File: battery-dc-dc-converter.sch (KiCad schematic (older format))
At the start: 26 parts, among them J1 Conn_01x02, J2 Conn_01x02, U1 LMR16030

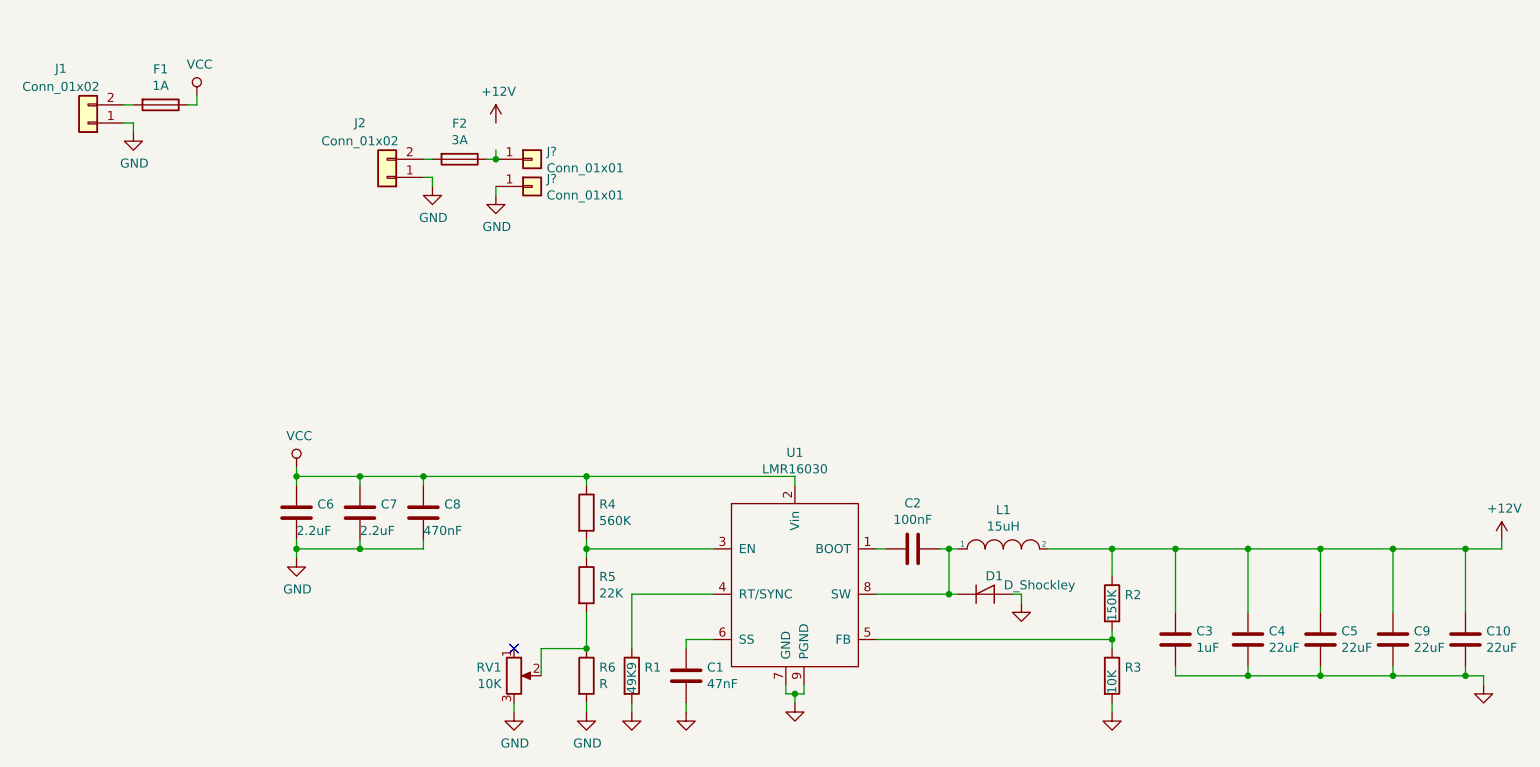
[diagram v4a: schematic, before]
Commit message: Panalized PCBs
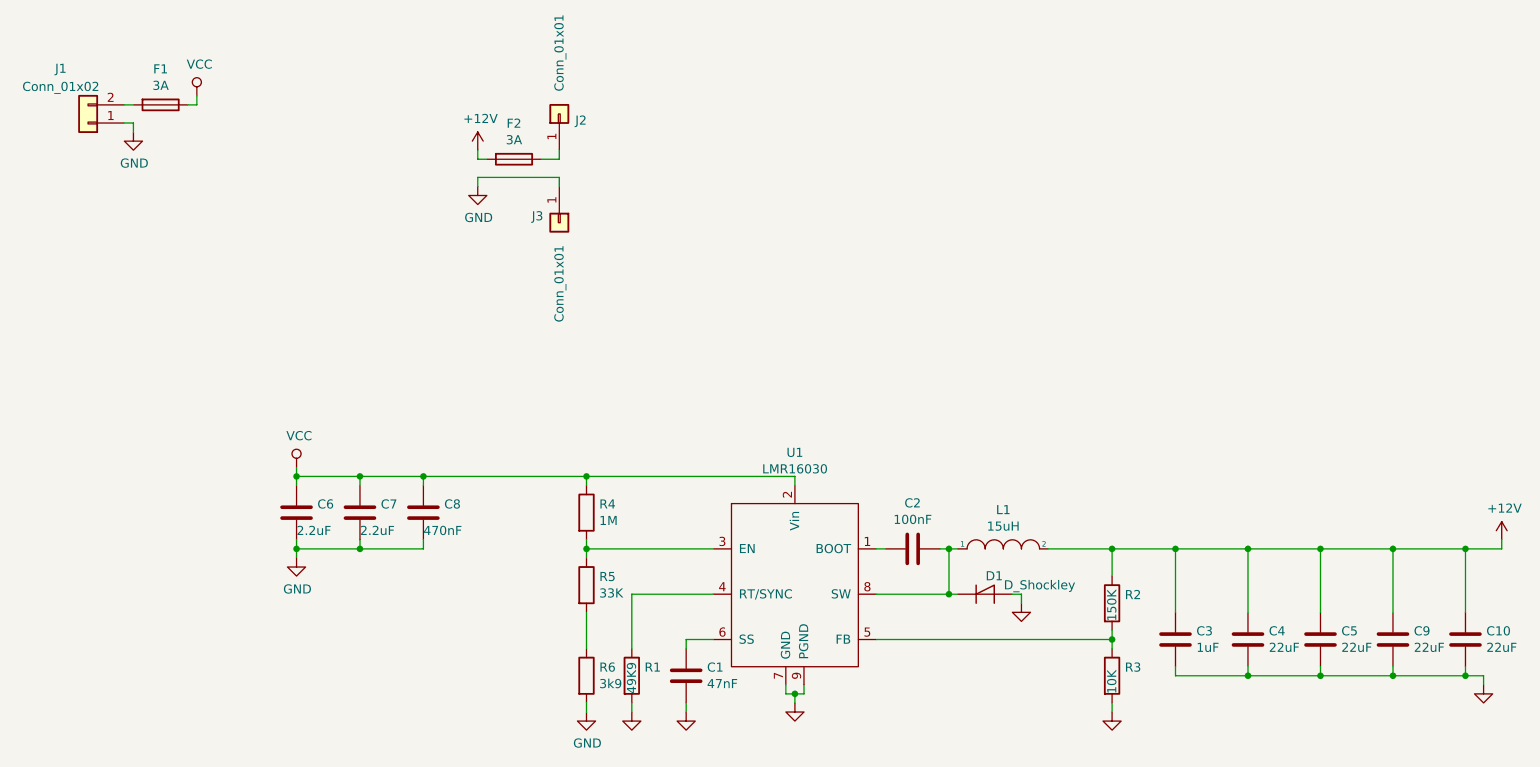
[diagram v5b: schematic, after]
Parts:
- removed J2: Conn_01x02, Connector_JST:JST_XH_B2B-XH-A_1x02_P2.50mm_Vertical, symbol Connector_Generic:Conn_01x02
- removed J? (x2): Conn_01x01, Connector_Wire:SolderWirePad_1x01_SMD_5x10mm, symbol Connector_Generic:Conn_01x01
- removed RV1: 10K, Potentiometer_THT:Potentiometer_Vishay_T73XX_Horizontal, symbol Device:R_POT
- added J2, J3: Conn_01x01, battery-dc-dc-converter:hole-pad, symbol Connector_Generic:Conn_01x01
- F1: value 1A -> 3A; LCSC C182305 -> C182441
- R4: value 560K -> 1M; LCSC C15785 -> C17514
- R5: value 22K -> 33K; LCSC C17560 -> C17633
- R6: value R -> 3k9; LCSC C17477 -> C17614
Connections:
- net +12V: now also F2.2
- net GND: now also J3.1 (Pin_1)
- net at F2.1: now also J2.1 (Pin_1)
- no-connect marks 1 -> 0
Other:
- moved on the sheet: F2
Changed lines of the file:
@@
 	1200 1000 1250 1000
-$Comp
-L Connector_Generic:Conn_01x02 J2
-U 1 1 5F4E1407
-P 2650 1400
-F 0 "J2" H 2800 1100 50  0000 C CNN
-F 1 "Conn_01x02" H 2800 1200 50  0000 C CNN
-F 2 "Connector_JST:JST_XH_B2B-XH-A_1x02_P2.50mm_Vertical" H 2650 1400 50  0001 C CNN
-F 3 "~" H 2650 1400 50  0001 C CNN
-F 4 "C8465" H 2650 1400 50  0001 C CNN "LCSC"
-	1    2650 1400
-	-1   0    0    1
-$EndComp
 $Comp
 L power:GND #PWR0111
 U 1 1 5F4E19F6
-P 2900 1450
-F 0 "#PWR0111" H 2900 1200 50  0001 C CNN
-F 1 "GND" H 2905 1277 50  0000 C CNN
-F 2 "" H 2900 1450 50  0001 C CNN
-F 3 "" H 2900 1450 50  0001 C CNN
-	1    2900 1450
+P 3150 1450
+F 0 "#PWR0111" H 3150 1200 50  0001 C CNN
+F 1 "GND" H 3155 1277 50  0000 C CNN
+F 2 "" H 3150 1450 50  0001 C CNN
+F 3 "" H 3150 1450 50  0001 C CNN
+	1    3150 1450
 	1    0    0    -1
 $EndComp
@@
 L power:+12V #PWR0112
 U 1 1 5F4E22CD
-P 3250 1100
-F 0 "#PWR0112" H 3250 950 50  0001 C CNN
-F 1 "+12V" H 3265 1273 50  0000 C CNN
-F 2 "" H 3250 1100 50  0001 C CNN
-F 3 "" H 3250 1100 50  0001 C CNN
-	1    3250 1100
-	1    0    0    -1
-$EndComp
-Wire Wire Line
-	2850 1300 2900 1300
-Wire Wire Line
-	2850 1400 2900 1400
-Wire Wire Line
-	2900 1400 2900 1450
+P 3150 1250
+F 0 "#PWR0112" H 3150 1100 50  0001 C CNN
+F 1 "+12V" H 3165 1423 50  0000 C CNN
+F 2 "" H 3150 1250 50  0001 C CNN
+F 3 "" H 3150 1250 50  0001 C CNN
+	1    3150 1250
+	1    0    0    -1
+$EndComp
 Wire Wire Line
 	1250 1100 1250 1150
@@
 P 1400 1000
 F 0 "F1" V 1203 1000 50  0000 C CNN
-F 1 "1A" V 1294 1000 50  0000 C CNN
+F 1 "3A" V 1294 1000 50  0000 C CNN
 F 2 "Fuse:Fuse_1206_3216Metric_Pad1.42x1.75mm_HandSolder" V 1330 1000 50  0001 C CNN
 F 3 "~" H 1400 1000 50  0001 C CNN
-F 4 "C182305" H 1400 1000 50  0001 C CNN "LCSC"
+F 4 "C182441" H 1400 1000 50  0001 C CNN "LCSC"
 	1    1400 1000
 	0    1    1    0
@@
 L Device:Fuse F2
 U 1 1 5FB27E6C
-P 3050 1300
-F 0 "F2" V 2853 1300 50  0000 C CNN
-F 1 "3A" V 2944 1300 50  0000 C CNN
-F 2 "Fuse:Fuse_1206_3216Metric_Pad1.42x1.75mm_HandSolder" V 2980 1300 50  0001 C CNN
-F 3 "~" H 3050 1300 50  0001 C CNN
-F 4 "C182441" H 3050 1300 50  0001 C CNN "LCSC"
-	1    3050 1300
+P 3350 1300
+F 0 "F2" V 3153 1300 50  0000 C CNN
+F 1 "3A" V 3244 1300 50  0000 C CNN
+F 2 "Fuse:Fuse_1206_3216Metric_Pad1.42x1.75mm_HandSolder" V 3280 1300 50  0001 C CNN
+F 3 "~" H 3350 1300 50  0001 C CNN
+F 4 "C182441" H 3350 1300 50  0001 C CNN "LCSC"
+	1    3350 1300
 	0    1    1    0
 $EndComp
-Wire Wire Line
-	3200 1300 3250 1300
-Wire Wire Line
-	3250 1300 3250 1250
 $Comp
 L Device:R R4
@@
 P 3750 3250
 F 0 "R4" H 3820 3296 50  0000 L CNN
-F 1 "560K" H 3820 3205 50  0000 L CNN
+F 1 "1M" H 3820 3205 50  0000 L CNN
 F 2 "Resistor_SMD:R_0805_2012Metric_Pad1.20x1.40mm_HandSolder" V 3680 3250 50  0001 C CNN
 F 3 "~" H 3750 3250 50  0001 C CNN
-F 4 "C15785" H 3750 3250 50  0001 C CNN "LCSC"
+F 4 "C17514" H 3750 3250 50  0001 C CNN "LCSC"
 	1    3750 3250
 	1    0    0    -1
@@
 P 3750 3650
 F 0 "R5" H 3820 3696 50  0000 L CNN
-F 1 "22K" H 3820 3605 50  0000 L CNN
+F 1 "33K" H 3820 3605 50  0000 L CNN
 F 2 "Resistor_SMD:R_0805_2012Metric_Pad1.20x1.40mm_HandSolder" V 3680 3650 50  0001 C CNN
 F 3 "~" H 3750 3650 50  0001 C CNN
-F 4 "C17560" H 3750 3650 50  0001 C CNN "LCSC"
+F 4 "C17633" H 3750 3650 50  0001 C CNN "LCSC"
 	1    3750 3650
 	1    0    0    -1
@@
 Wire Wire Line
 	4900 3050 4900 3100
-$Comp
-L Device:R_POT RV1
-U 1 1 5FB5C125
-P 3350 4150
-F 0 "RV1" H 3281 4196 50  0000 R CNN
-F 1 "10K" H 3281 4105 50  0000 R CNN
-F 2 "Potentiometer_THT:Potentiometer_Vishay_T73XX_Horizontal" H 3350 4150 50  0001 C CNN
-F 3 "~" H 3350 4150 50  0001 C CNN
-F 4 "C118898" H 3350 4150 50  0001 C CNN "LCSC"
-	1    3350 4150
-	1    0    0    -1
-$EndComp
-NoConn ~ 3350 4000
 Wire Wire Line
 	3750 4000 3750 3800
@@
 P 3750 4150
 F 0 "R6" H 3820 4196 50  0000 L CNN
-F 1 "R" H 3820 4105 50  0000 L CNN
+F 1 "3k9" H 3820 4105 50  0000 L CNN
 F 2 "Resistor_SMD:R_0805_2012Metric_Pad1.20x1.40mm_HandSolder" V 3680 4150 50  0001 C CNN
 F 3 "~" H 3750 4150 50  0001 C CNN
-F 4 "C17477" H 3750 4150 50  0001 C CNN "LCSC"
+F 4 "C17614" H 3750 4150 50  0001 C CNN "LCSC"
 	1    3750 4150
 	1    0    0    -1
 $EndComp
-Connection ~ 3750 4000
-Wire Wire Line
-	3500 4000 3500 4150
-Wire Wire Line
-	3500 4000 3750 4000
-$Comp
-L power:GND #PWR0115
-U 1 1 5FB7F217
-P 3350 4350
-F 0 "#PWR0115" H 3350 4100 50  0001 C CNN
-F 1 "GND" H 3355 4177 50  0000 C CNN
-F 2 "" H 3350 4350 50  0001 C CNN
-F 3 "" H 3350 4350 50  0001 C CNN
-	1    3350 4350
-	1    0    0    -1
-$EndComp
 Wire Wire Line
 	3750 4300 3750 4350
-Wire Wire Line
-	3350 4350 3350 4300
-$Comp
-L Connector_Generic:Conn_01x01 J?
-U 1 1 60369738
-P 3450 1300
-F 0 "J?" H 3530 1342 50  0000 L CNN
-F 1 "Conn_01x01" H 3530 1251 50  0000 L CNN
-F 2 "Connector_Wire:SolderWirePad_1x01_SMD_5x10mm" H 3450 1300 50  0001 C CNN
-F 3 "~" H 3450 1300 50  0001 C CNN
-	1    3450 1300
-	1    0    0    -1
-$EndComp
-Connection ~ 3250 1300
-$Comp
-L Connector_Generic:Conn_01x01 J?
-U 1 1 60369BF3
-P 3450 1450
-F 0 "J?" H 3530 1492 50  0000 L CNN
-F 1 "Conn_01x01" H 3530 1401 50  0000 L CNN
-F 2 "Connector_Wire:SolderWirePad_1x01_SMD_5x10mm" H 3450 1450 50  0001 C CNN
-F 3 "~" H 3450 1450 50  0001 C CNN
-	1    3450 1450
-	1    0    0    -1
-$EndComp
-$Comp
-L power:GND #PWR?
-U 1 1 6036A147
-P 3250 1500
-F 0 "#PWR?" H 3250 1250 50  0001 C CNN
-F 1 "GND" H 3255 1327 50  0000 C CNN
-F 2 "" H 3250 1500 50  0001 C CNN
-F 3 "" H 3250 1500 50  0001 C CNN
-	1    3250 1500
-	1    0    0    -1
-$EndComp
-Wire Wire Line
-	3250 1500 3250 1450
+$Comp
+L Connector_Generic:Conn_01x01 J2
+U 1 1 603798F3
+P 3600 1050
+F 0 "J2" V 3564 962 50  0000 R CNN
+F 1 "Conn_01x01" H 4150 1050 50  0000 R CNN
+F 2 "battery-dc-dc-converter:hole-pad" H 3600 1050 50  0001 C CNN
+F 3 "~" H 3600 1050 50  0001 C CNN
+	1    3600 1050
+	0    -1   -1   0
+$EndComp
+$Comp
+L Connector_Generic:Conn_01x01 J3
+U 1 1 6037DD21
+P 3600 1650
+F 0 "J3" V 3564 1562 50  0000 R CNN
+F 1 "Conn_01x01" H 4150 1650 50  0000 R CNN
+F 2 "battery-dc-dc-converter:hole-pad" H 3600 1650 50  0001 C CNN
+F 3 "~" H 3600 1650 50  0001 C CNN
+	1    3600 1650
+	0    1    1    0
+$EndComp
+Wire Wire Line
+	3150 1450 3150 1400
+Wire Wire Line
+	3150 1400 3600 1400
+Wire Wire Line
+	3600 1400 3600 1450
+Wire Wire Line
+	3150 1250 3150 1300
+Wire Wire Line
+	3150 1300 3200 1300
+Wire Wire Line
+	3500 1300 3600 1300
+Wire Wire Line
+	3600 1300 3600 1250
 $EndSCHEMATC

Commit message: Improved EMI
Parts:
- removed C10, C9: 22uF, Capacitor_SMD:C_0805_2012Metric, symbol Device:C
- added R7: 3R3, Resistor_SMD:R_0805_2012Metric, symbol Device:R
- C10: renamed from C6; footprint Capacitor_SMD:C_1206_3216Metric -> Capacitor_SMD:C_1210_3225Metric; LCSC C50254 -> C106115
- C11: renamed from C7; footprint Capacitor_SMD:C_1206_3216Metric -> Capacitor_SMD:C_1210_3225Metric; LCSC C50254 -> C106115
- C12: renamed from C8; LCSC C13967 -> C513710
- L1: footprint scooter-ps:MWSA1004 -> battery-dc-dc-converter:SWRH1207B; LCSC C151872 -> C115137
- U1: footprint Package_SO:HTSOP-8-1EP_3.9x4.9mm_P1.27mm_EP2.4x3.2mm_ThermalVias -> Package_SO:HTSOP-8-1EP_3.9x4.9mm_P1.27mm_EP2.4x3.2mm
- renumbered C4 to C1, C5 to C2, C1 to C3, C2 to C4, C3 to C7
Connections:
- net at D1.1 (K), L1.1, U1.8 (SW): now also R7.1; no longer C4.1
- new net: C4.1, R7.2
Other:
- note added: "Boot R"
- moved on the sheet: C1, C2, C7, D1, L1, R2, R3

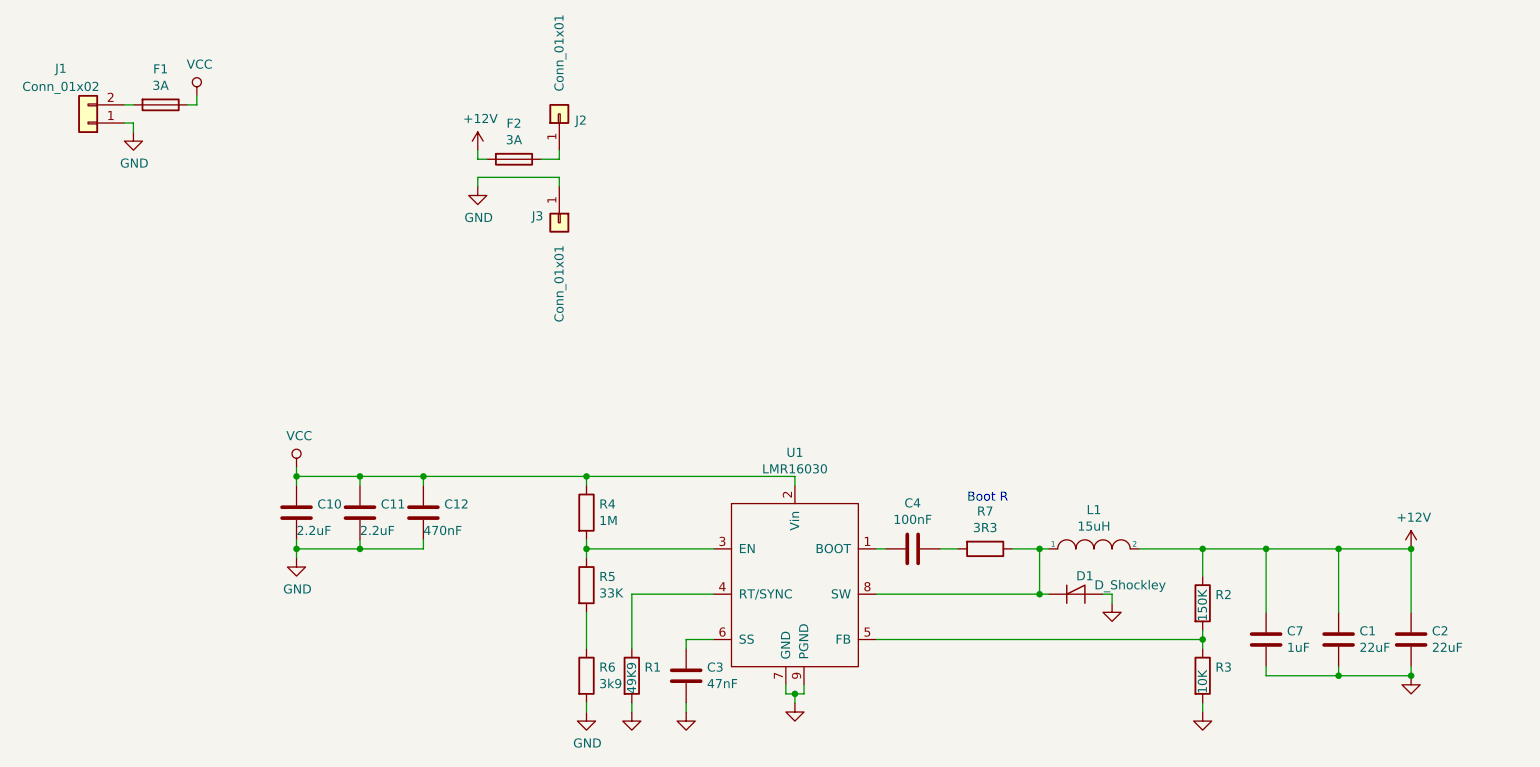
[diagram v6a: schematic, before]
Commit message: Added lmr16020
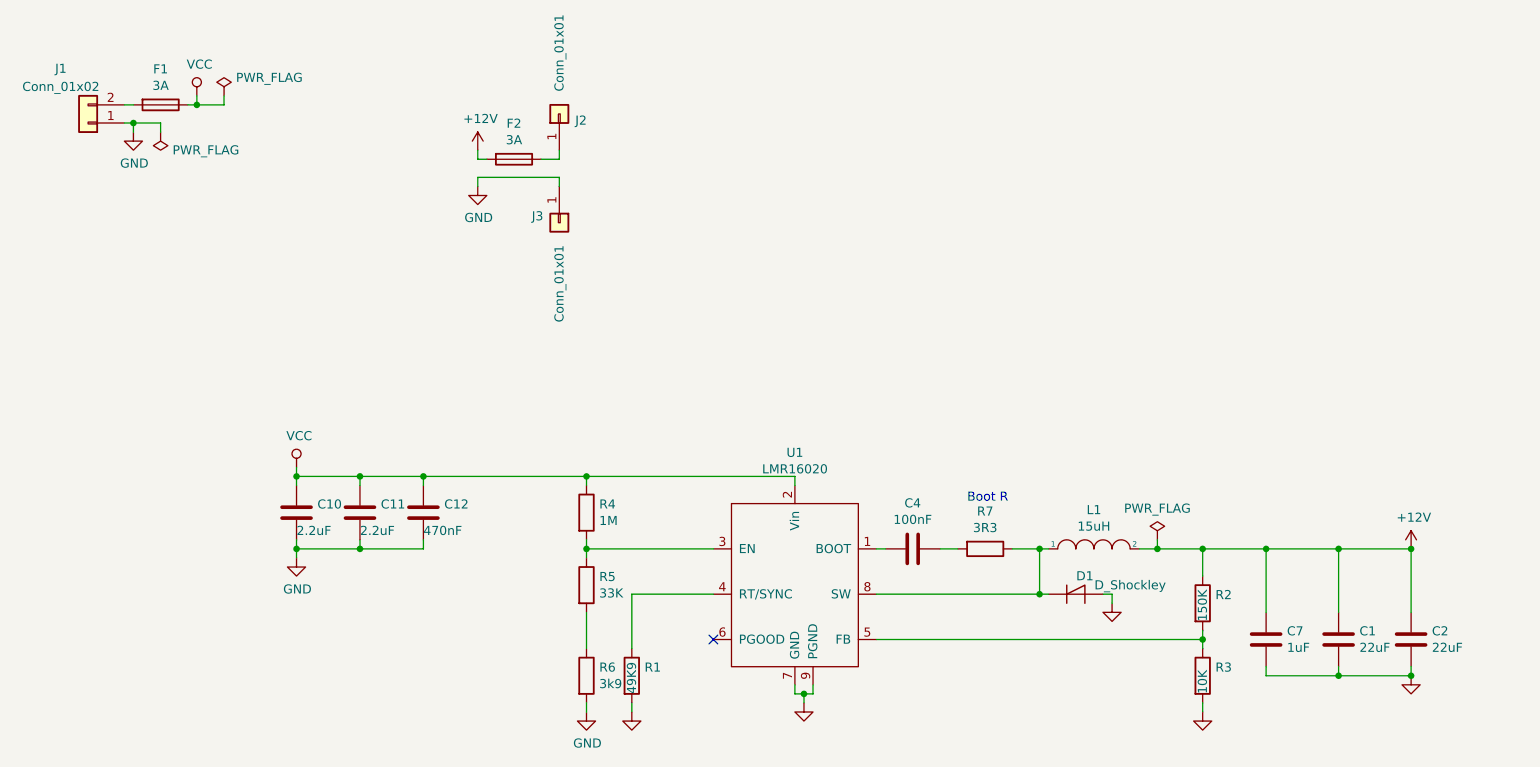
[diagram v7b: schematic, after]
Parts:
- removed C3: 47nF, Capacitor_SMD:C_0603_1608Metric, symbol Device:C
- removed U1: LMR16030, Package_SO:HTSOP-8-1EP_3.9x4.9mm_P1.27mm_EP2.4x3.2mm, symbol scooter-ps:LMR16030
- added U1: LMR16020, Package_SO:HTSOP-8-1EP_3.9x4.9mm_P1.27mm_EP2.4x3.2mm, symbol scooter-ps:LMR16020
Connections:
- net GND: now also U1.7 (GND), U1.9 (PGND)
- net VCC: now also U1.2 (Vin)
- net at C4.2: now also U1.1 (BOOT)
- net at R4.2, R5.1: now also U1.3 (EN)
- net at R1.1: now also U1.4 (RT/SYNC)
- net at R2.2, R3.1: now also U1.5 (FB)
- net at D1.1 (K), L1.1, R7.1: now also U1.8 (SW)
- no-connect marks 0 -> 1
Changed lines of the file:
@@
 $EndDescr
-$Comp
-L scooter-ps:LMR16030 U1
-U 1 1 5F4707DD
-P 4900 3800
-F 0 "U1" H 4900 4681 50  0000 C CNN
-F 1 "LMR16030" H 4900 4590 50  0000 C CNN
-F 2 "Package_SO:HTSOP-8-1EP_3.9x4.9mm_P1.27mm_EP2.4x3.2mm" H 4900 3800 50  0001 C CNN
-F 3 "" H 4900 3800 50  0001 C CNN
-F 4 "C90665" H 4900 3800 50  0001 C CNN "LCSC"
-	1    4900 3800
-	1    0    0    -1
-$EndComp
 $Comp
 L power:GND #PWR0101
 U 1 1 5F470A9D
-P 4900 4300
-F 0 "#PWR0101" H 4900 4050 50  0001 C CNN
-F 1 "GND" H 4905 4127 50  0001 C CNN
-F 2 "" H 4900 4300 50  0001 C CNN
-F 3 "" H 4900 4300 50  0001 C CNN
-	1    4900 4300
-	1    0    0    -1
-$EndComp
-Wire Wire Line
-	4850 4200 4850 4250
-Wire Wire Line
-	4850 4250 4900 4250
-Wire Wire Line
-	4950 4250 4950 4200
-Wire Wire Line
-	4900 4300 4900 4250
-Connection ~ 4900 4250
+P 4950 4300
+F 0 "#PWR0101" H 4950 4050 50  0001 C CNN
+F 1 "GND" H 4955 4127 50  0001 C CNN
+F 2 "" H 4950 4300 50  0001 C CNN
+F 3 "" H 4950 4300 50  0001 C CNN
+	1    4950 4300
+	1    0    0    -1
+$EndComp
+Wire Wire Line
+	4900 4200 4900 4250
 Wire Wire Line
 	4900 4250 4950 4250
-$Comp
-L Device:C C3
-U 1 1 5F470DF7
-P 4300 4150
-F 0 "C3" H 4415 4196 50  0000 L CNN
-F 1 "47nF" H 4415 4105 50  0000 L CNN
-F 2 "Capacitor_SMD:C_0603_1608Metric" H 4338 4000 50  0001 C CNN
-F 3 "~" H 4300 4150 50  0001 C CNN
-F 4 "C1622" H 4300 4150 50  0001 C CNN "LCSC"
-	1    4300 4150
-	1    0    0    -1
-$EndComp
+Wire Wire Line
+	5000 4250 5000 4200
+Wire Wire Line
+	4950 4300 4950 4250
+Connection ~ 4950 4250
+Wire Wire Line
+	4950 4250 5000 4250
 $Comp
 L Device:R R1
@@
 $EndComp
 $Comp
-L power:GND #PWR0102
-U 1 1 5F471419
-P 4300 4350
-F 0 "#PWR0102" H 4300 4100 50  0001 C CNN
-F 1 "GND" H 4305 4177 50  0001 C CNN
-F 2 "" H 4300 4350 50  0001 C CNN
-F 3 "" H 4300 4350 50  0001 C CNN
-	1    4300 4350
-	1    0    0    -1
-$EndComp
-$Comp
 L power:GND #PWR0103
 U 1 1 5F471545
@@
 	1    0    0    -1
 $EndComp
-Wire Wire Line
-	4300 4350 4300 4300
-Wire Wire Line
-	4300 4000 4300 3950
-Wire Wire Line
-	4300 3950 4450 3950
 Wire Wire Line
 	4000 3700 4000 4000
@@
 Connection ~ 7150 3950
 Wire Wire Line
-	6800 3450 7150 3450
+	6800 3450 6900 3450
 Wire Wire Line
 	7500 3450 7500 3800
@@
 	1    0    0    -1
 $EndComp
-$Comp
-L power:+12V #PWR0112
-U 1 1 5F4E22CD
-P 3150 1250
-F 0 "#PWR0112" H 3150 1100 50  0001 C CNN
-F 1 "+12V" H 3165 1423 50  0000 C CNN
-F 2 "" H 3150 1250 50  0001 C CNN
-F 3 "" H 3150 1250 50  0001 C CNN
-	1    3150 1250
-	1    0    0    -1
-$EndComp
 Wire Wire Line
 	1250 1100 1250 1150
@@
 Connection ~ 8300 4150
 Connection ~ 8300 3450
+NoConn ~ 4450 3950
+$Comp
+L scooter-ps:LMR16020 U1
+U 1 1 616BFB88
+P 4900 3800
+F 0 "U1" H 4900 4681 50  0000 C CNN
+F 1 "LMR16020" H 4900 4590 50  0000 C CNN
+F 2 "Package_SO:HTSOP-8-1EP_3.9x4.9mm_P1.27mm_EP2.4x3.2mm" H 4900 3800 50  0001 C CNN
+F 3 "" H 4900 3800 50  0001 C CNN
+	1    4900 3800
+	1    0    0    -1
+$EndComp
+$Comp
+L power:PWR_FLAG #FLG0101
+U 1 1 616C8A6D
+P 6900 3400
+F 0 "#FLG0101" H 6900 3475 50  0001 C CNN
+F 1 "PWR_FLAG" H 6900 3573 50  0000 C CNN
+F 2 "" H 6900 3400 50  0001 C CNN
+F 3 "~" H 6900 3400 50  0001 C CNN
+	1    6900 3400
+	1    0    0    -1
+$EndComp
+Wire Wire Line
+	6900 3400 6900 3450
+Connection ~ 6900 3450
+Wire Wire Line
+	6900 3450 7150 3450
+$Comp
+L power:+12V #PWR0112
+U 1 1 5F4E22CD
+P 3150 1250
+F 0 "#PWR0112" H 3150 1100 50  0001 C CNN
+F 1 "+12V" H 3165 1423 50  0000 C CNN
+F 2 "" H 3150 1250 50  0001 C CNN
+F 3 "" H 3150 1250 50  0001 C CNN
+	1    3150 1250
+	1    0    0    -1
+$EndComp
+$Comp
+L power:PWR_FLAG #FLG0102
+U 1 1 616CFDC9
+P 1400 1150
+F 0 "#FLG0102" H 1400 1225 50  0001 C CNN
+F 1 "PWR_FLAG" H 1150 1250 50  0000 C CNN
+F 2 "" H 1400 1150 50  0001 C CNN
+F 3 "~" H 1400 1150 50  0001 C CNN
+	1    1400 1150
+	-1   0    0    1
+$EndComp
+$Comp
+L power:PWR_FLAG #FLG0103
+U 1 1 616D16FE
+P 1750 950
+F 0 "#FLG0103" H 1750 1025 50  0001 C CNN
+F 1 "PWR_FLAG" H 2000 1050 50  0000 C CNN
+F 2 "" H 1750 950 50  0001 C CNN
+F 3 "~" H 1750 950 50  0001 C CNN
+	1    1750 950
+	1    0    0    -1
+$EndComp
+Wire Wire Line
+	1600 1000 1750 1000
+Wire Wire Line
+	1750 1000 1750 950
+Connection ~ 1600 1000
+Wire Wire Line
+	1250 1100 1400 1100
+Wire Wire Line
+	1400 1100 1400 1150
+Connection ~ 1250 1100
 $EndSCHEMATC
